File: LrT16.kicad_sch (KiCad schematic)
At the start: 160 parts, among them J1 USB_C_Receptacle_USB2.0, J2 Conn_02x07_Odd_Even, Q1 2N7002, Q2 2N7002, SW1 EC11_SMD, SW10 EC11_SMD, SW11 EC11_SMD, SW12 EC11_SMD, SW13 EC11_SMD, SW14 EC11_SMD, SW15 EC11_SMD, SW16 EC11_SMD, SW17 SW_Push, SW18 SW_Push, SW19 SW_SPST, SW2 EC11_SMD, SW3 EC11_SMD, SW4 EC11_SMD, SW5 EC11_SMD, SW6 EC11_SMD, SW7 EC11_SMD, SW8 EC11_SMD, SW9 EC11_SMD, U1 STM32F072R8Tx, U2 SPX3819M5-L3-3TR

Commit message: middle of PCB work
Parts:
- removed C33: 100n, Capacitor_SMD:C_0603_1608Metric, symbol LrE-6-rescue:C-Device
- C35, C37, C39, C41, C42: footprint Capacitor_SMD:C_0603_1608Metric -> Capacitor_SMD:C_0402_1005Metric
- C36, C38, C40, C43: footprint Capacitor_SMD:C_0805_2012Metric -> Capacitor_SMD:C_0402_1005Metric
- J2: footprint (none) -> Connector_PinHeader_1.27mm:PinHeader_2x07_P1.27mm_Horizontal
- R35, R36: footprint Resistor_SMD:R_0603_1608Metric -> Resistor_SMD:R_0402_1005Metric
- R37, R38: footprint Resistor_SMD:R_0805_2012Metric -> Resistor_SMD:R_0805_2012Metric_Pad1.20x1.40mm_HandSolder
- renumbered D9 to D11, D11 to D12, D15 to D14, D14 to D15, D12 to D9, SW1 to SW0, SW2 to SW1, SW11 to SW10, SW12 to SW11, SW13 to SW12, SW14 to SW13, SW15 to SW14, SW16 to SW15, SW3 to SW2, SW5 to SW3, SW6 to SW5, SW7 to SW6, SW8 to SW7, SW9 to SW8, SW10 to SW9
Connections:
- net SW17: now also U1.21 (PA5); no longer U1.23 (PA7)
- net SW18: now also U1.20 (PA4); no longer U1.43 (PA10)

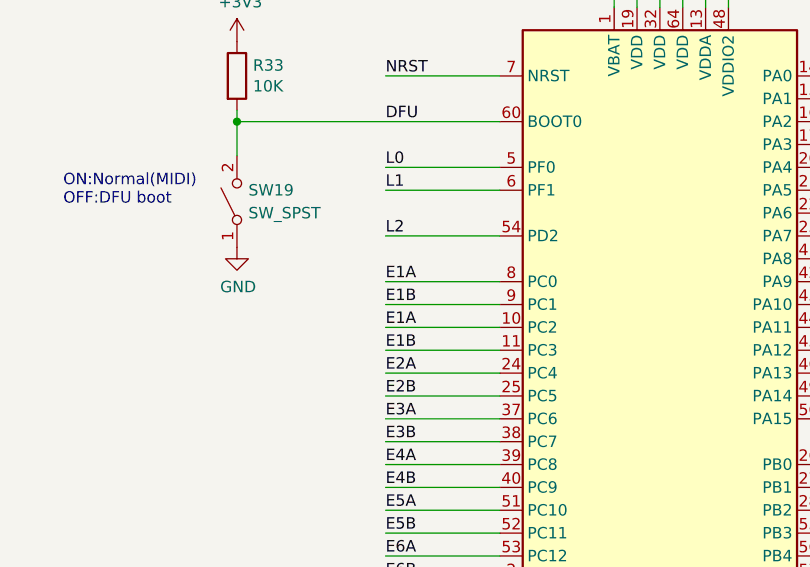
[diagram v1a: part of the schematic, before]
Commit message: mod. J2 footprint
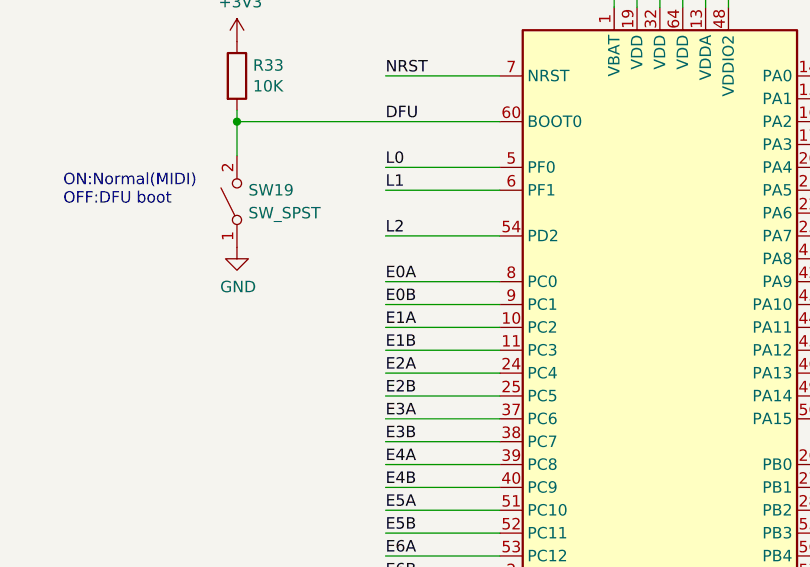
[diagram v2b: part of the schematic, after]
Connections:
- net E0A: now also U1.8 (PC0)
- net E0B: now also U1.9 (PC1)
- net E1A: no longer U1.8 (PC0)
- net E1B: no longer U1.9 (PC1)
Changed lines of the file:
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@@
 		)
 	)
-	(label "E1B"
+	(label "E0B"
 		(at 256.54 104.14 0)
 		(effects
@@
 		)
 	)
-	(label "E1A"
+	(label "E0A"
 		(at 256.54 101.6 0)
 		(effects

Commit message: reduce 3.3v fill area
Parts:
- R39, R40: footprint Resistor_SMD:R_0805_2012Metric -> Resistor_SMD:R_0603_1608Metric
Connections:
- net GND: now also SW18.2; no longer SW18.1
- net SW18: now also SW18.1; no longer SW18.2
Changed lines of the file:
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@@
 			)
 		)
-		(property "Footprint" "Resistor_SMD:R_0805_2012Metric"
+		(property "Footprint" "Resistor_SMD:R_0603_1608Metric"
 			(at 496.062 154.94 90)
 			(effects
@@
 			)
 		)
-		(property "Footprint" "Resistor_SMD:R_0805_2012Metric"
+		(property "Footprint" "Resistor_SMD:R_0603_1608Metric"
 			(at 497.332 115.57 90)
 			(effects
@@
 		(lib_id "Switch:SW_Push")
 		(at 486.41 161.29 0)
+		(mirror y)
 		(unit 1)
 		(exclude_from_sim no)
@@
 		(on_board yes)
 		(dnp no)
-		(fields_autoplaced yes)
 		(property "Reference" "SW18"
 			(at 486.41 153.67 0)

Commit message: eliminate errors and warnings
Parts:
- renumbered REF1 to REF01
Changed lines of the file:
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@@
 		(dnp no)
 		(fields_autoplaced yes)
-		(property "Reference" "REF1"
+		(property "Reference" "REF01"
 			(at 482.6 360.6799 0)
 			(effects
@@
 			(project "LrT16"
 				(path "/b873bc5d-a9af-4bd9-afcb-87ce4d417120"
-					(reference "REF1")
+					(reference "REF01")
 					(unit 1)
 				)

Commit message: F2.0 board ordered.
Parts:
- J2, U1: now left out of the parts list
- R33, R41: footprint Resistor_SMD:R_0805_2012Metric -> Resistor_SMD:R_0603_1608Metric
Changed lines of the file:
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@@
 			)
 		)
-		(property "Footprint" "Resistor_SMD:R_0805_2012Metric"
+		(property "Footprint" "Resistor_SMD:R_0603_1608Metric"
 			(at 526.542 208.28 90)
 			(effects
@@
 			)
 		)
-		(property "Footprint" "Resistor_SMD:R_0805_2012Metric"
+		(property "Footprint" "Resistor_SMD:R_0603_1608Metric"
 			(at 238.252 78.74 90)
 			(effects
@@
 		(unit 1)
 		(exclude_from_sim no)
-		(in_bom yes)
+		(in_bom no)
 		(on_board yes)
 		(dnp no)
@@
 		(unit 1)
 		(exclude_from_sim no)
-		(in_bom yes)
+		(in_bom no)
 		(on_board yes)
 		(dnp no)
